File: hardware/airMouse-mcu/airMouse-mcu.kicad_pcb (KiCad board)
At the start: 2 copper layers, 56.5 x 64.5 mm, 115 parts, among them J1 MCU_PRG, J2 RADIO_PRG, J3 AT, J4 DS1020-07-16VBT1A-R, J5 DS1020-07-10VBT1A-R, J6 DS1020-07-4VBT1A-R, Q1 IRLML6346, SW1 KEY, U1 LSM6DS3TR-C, U2 MCP1640CT-I/CHY, U3 STM32G071RBTx, U4 ESP32-C3-WROOM-02U

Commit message: updated for kicad 9
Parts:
- R19: value 2k2 -> 0R
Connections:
- C27 pad 1: /mouse/MOUSE_HOME -> /mouse/MOUSE_BACK
- C28 pad 1: /mouse/MOUSE_PRC -> /mouse/MOUSE_FWD
- C30 pad 1: /mouse/MOUSE_BACK -> /mouse/MOUSE_HOME
- C31 pad 1: /mouse/MOUSE_FWD -> /mouse/MOUSE_PRC
- R50 pad 2: /mouse/MOUSE_FWD -> /mouse/MOUSE_PRC
- R51 pad 2: /mouse/MOUSE_BACK -> /mouse/MOUSE_HOME
- R53 pad 2: /mouse/MOUSE_PRC -> /mouse/MOUSE_FWD
- R54 pad 2: /mouse/MOUSE_HOME -> /mouse/MOUSE_BACK
- U3 pad 1: /mouse/MOUSE_FWD -> /mouse/MOUSE_PRC
- U3 pad 2: /mouse/MOUSE_BACK -> /mouse/MOUSE_HOME
- U3 pad 4: /mouse/MOUSE_PRC -> /mouse/MOUSE_FWD
- U3 pad 5: /mouse/MOUSE_HOME -> /mouse/MOUSE_BACK
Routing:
- net /mouse/MOUSE_HOME: track 48.5 -> 27.4 mm
- net /mouse/MOUSE_BACK: track 27.4 -> 48.5 mm
- net /mouse/MOUSE_PRC: track 48.0 -> 28.9 mm
- net /mouse/MOUSE_FWD: track 28.9 -> 48.0 mm

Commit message: dont know, why voltage drops
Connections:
- net /ESP_RST renamed /ESP_EN
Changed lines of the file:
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@@
 	(net 93 "/COL2")
 	(net 94 "/COL1")
-	(net 95 "/ESP_RST")
+	(net 95 "/ESP_EN")
 	(net 96 "/FB")
 	(net 97 "GND")
@@
 			(size 1.5 0.9)
 			(layers "F.Cu" "F.Mask" "F.Paste")
-			(net 95 "/ESP_RST")
+			(net 95 "/ESP_EN")
 			(pinfunction "EN")
 			(pintype "input")
@@
 			(layers "F.Cu" "F.Mask" "F.Paste")
 			(roundrect_rratio 0.25)
-			(net 95 "/ESP_RST")
+			(net 95 "/ESP_EN")
 			(pinfunction "PB15")
 			(pintype "bidirectional")
@@
 			(layers "F.Cu" "F.Mask" "F.Paste")
 			(roundrect_rratio 0.25)
-			(net 95 "/ESP_RST")
+			(net 95 "/ESP_EN")
 			(pintype "passive")
 		)
@@
 			(layers "F.Cu" "F.Mask" "F.Paste")
 			(roundrect_rratio 0.25)
-			(net 95 "/ESP_RST")
+			(net 95 "/ESP_EN")
 			(pintype "passive")
 		)

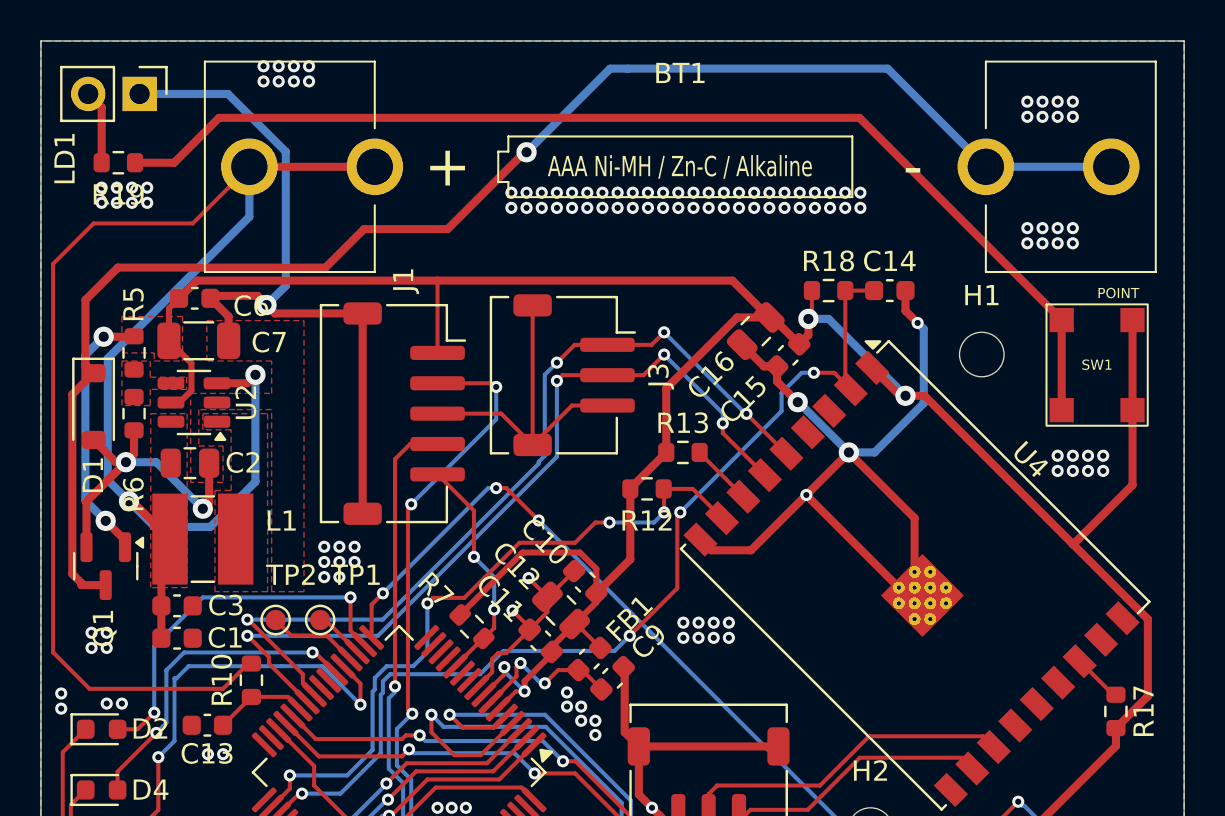
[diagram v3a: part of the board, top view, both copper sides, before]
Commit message: fixed receiving data- overrun turned off
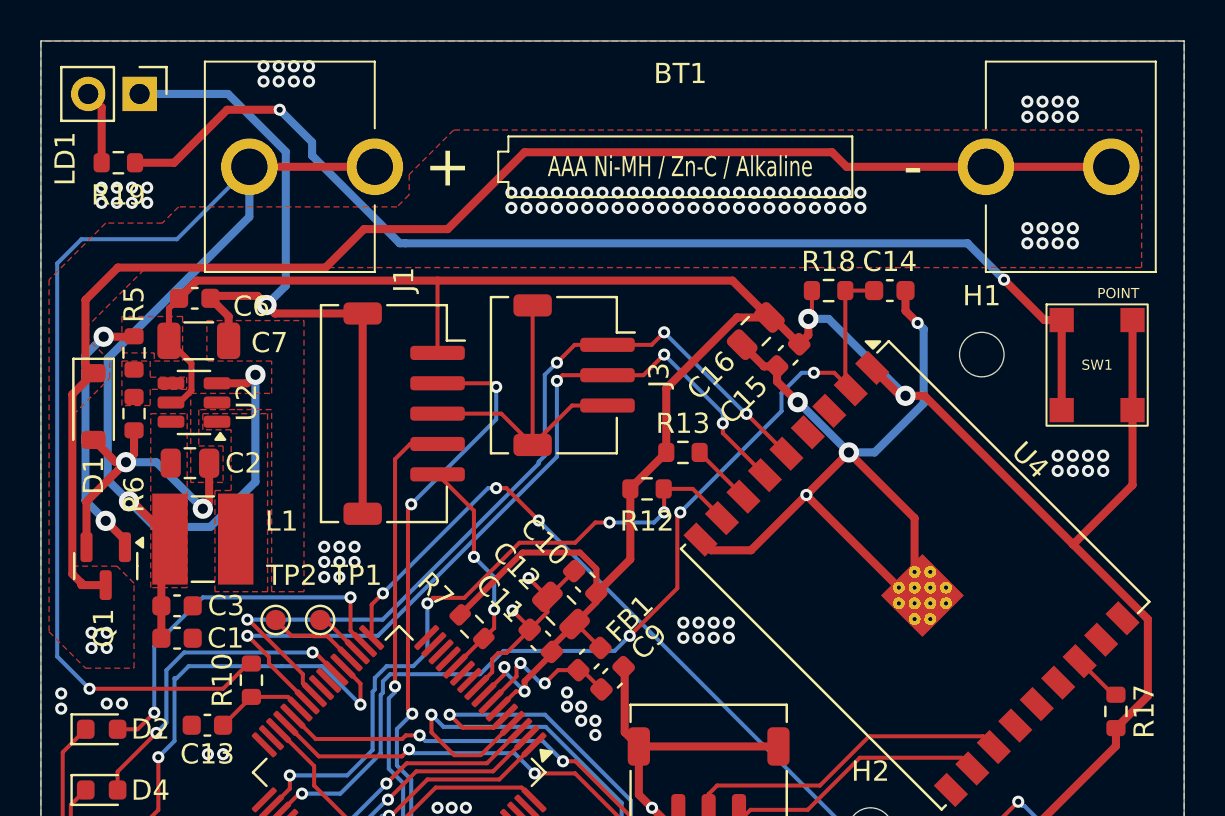
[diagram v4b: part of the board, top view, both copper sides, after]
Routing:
- net /BAT-: track 73.5 -> 70.1 mm, vias 1 -> 0
- net Net-(SW1-A): track 55.5 -> 56.3 mm, vias 0 -> 2
- net /BAT+: track 90.9 -> 90.6 mm, vias 2 -> 3
- added copper zone on F.Cu, net /BAT-

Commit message: new mcu pcb
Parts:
- removed C17, C18, C19, C20, C21, C22, C23, C24, C25, C26, C27, C28, C29, C30, C31, C32, C33, C34, C35, C36: 100n, Capacitor_SMD:C_0603_1608Metric
- removed H1, H2, H3: MountingHole, MountingHole:MountingHole_2.2mm_M2_ISO14580
- removed J3: AT, airMouseLib:JST_ZH_S3B-ZR-SM4A-TF_1x03-1MP_P1.50mm_Horizontal
- removed R26, R27, R28, R29, R30, R31, R32, R33, R34, R35, R36, R37, R38, R39, R40, R41, R42, R43, R44, R45, R46, R47, R48, R49, R50, R51, R52, R53, R54: 10k, Resistor_SMD:R_0603_1608Metric
- removed U4: ESP32-C3-WROOM-02U, RF_Module:ESP32-C3-WROOM-02U
- added C8: 100n, Capacitor_SMD:C_0603_1608Metric, B.Cu at (142.2, 113.6)
- added R55: 0R, Resistor_SMD:R_0603_1608Metric, F.Cu at (142.4, 78.2)
- added TP3: AT_MCU_RX, TestPoint:TestPoint_Pad_D1.0mm, F.Cu at (176.9, 90.5)
- added TP4: AT_MCU_TX, TestPoint:TestPoint_Pad_D1.0mm, F.Cu at (176.9, 93.6)
- added U5: ESP32-C3-WROOM-02, RF_Module:ESP32-C3-WROOM-02, F.Cu at (154.3, 83.8)
- C10, C11, C12, C14, C15, C16, C4, C5, C9, FB1, J2, J5, J6, R1, R11, R12, R13, R17, R19, R2, R25, R3, R4, R7, R8, R9, SW1, TP1, TP2, U1, U3: moved to B.Cu
- C7: footprint Capacitor_SMD:C_1206_3216Metric -> Capacitor_SMD:C_0805_2012Metric
- R18: value 10k -> 10k(NM); moved to B.Cu
- R5: value 976k -> 1M
- R6: value 562k -> 180k
- U2: value MCP1640CT-I/CHY -> TLV61070ADBV
- moved TP2 69.4 mm to (176.8, 84.9)
- moved D2 68.8 mm to (166.4, 87.2)
- moved D3 68.8 mm to (166.4, 93.2)
- moved D4 68.8 mm to (166.4, 90.2)
- moved R14 67.8 mm to (166.3, 100.9), turned to 180 degrees
- moved R16 66.7 mm to (166.3, 102.5), turned to 180 degrees
- moved R15 65.8 mm to (166.3, 104.1), turned to 180 degrees
- moved TP1 65.3 mm to (174.6, 84.9)
- moved LD1 61.6 mm to (166.4, 79.6), turned to 0 degrees
- moved R19 58.7 mm to (162.4, 82.2), turned to 180 degrees
- moved C13 53.0 mm to (157.8, 95.1)
- moved R11 52.6 mm to (162.5, 102.7), turned to -135 degrees
- moved R10 50.7 mm to (157.8, 93.6), turned to 180 degrees
- moved D1 48.4 mm to (150.7, 103.6), turned to 90 degrees
- moved Q1 48.0 mm to (150.1, 95.7), turned to 90 degrees
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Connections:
- C10 pad 1: +3V3 -> /MCU_3V3
- C11 pad 1: +3V3 -> /MCU_3V3
- C12 pad 1: +3V3 -> /MCU_3V3
- C15 pad 1: +3V3 -> /ESP_3V3
- C16 pad 1: +3V3 -> /ESP_3V3
- C4 pad 1: +3V3 -> /SENSOR_3V3
- C5 pad 1: +3V3 -> /SENSOR_3V3
- FB1 pad 1: +3V3 -> /MCU_3V3
- J4 pad 10: /Keyboard/COL6 -> /COL6
- J4 pad 11: /Keyboard/COL5 -> /COL5
- J4 pad 12: /Keyboard/COL4 -> /COL4
- J4 pad 13: /Keyboard/COL3 -> /COL3
- J4 pad 14: /Keyboard/COL2 -> /COL2
- J4 pad 15: /Keyboard/COL1 -> /COL1
- J4 pad 6: /Keyboard/COL10 -> /COL10
- J4 pad 7: /Keyboard/COL9 -> /COL9
- J4 pad 8: /Keyboard/COL8 -> /COL8
- J4 pad 9: /Keyboard/COL7 -> /COL7
- J5 pad 2: /mouse/HOME -> /mouse/MOUSE_DPI
- J5 pad 3: /mouse/PRECISION -> /mouse/MOUSE_HOME
- J5 pad 4: /mouse/DPI -> /mouse/MOUSE_PRC
- J5 pad 5: /mouse/SCRLDN -> /mouse/MOUSE_DN
- J5 pad 6: /mouse/SCRLUP -> /mouse/MOUSE_UP
- J5 pad 7: /mouse/RMB -> /mouse/MOUSE_RB
- J5 pad 8: /mouse/MMB -> /mouse/MOUSE_MB
- J5 pad 9: /mouse/LMB -> Net-(J5-Pin_9)
- J6 pad 2: /mouse/BACK -> /mouse/MOUSE_BACK
- J6 pad 3: /mouse/FWD -> /mouse/MOUSE_FWD
- R1 pad 1: +3V3 -> /SENSOR_3V3
- R12 pad 1: +3V3 -> /ESP_3V3
- R13 pad 1: +3V3 -> /ESP_3V3
- R17 pad 1: +3V3 -> /ESP_3V3
- R18 pad 1: +3V3 -> /ESP_3V3
- R25 pad 1: +3V3 -> Net-(J5-Pin_9)
- R25 pad 2: /Keyboard/COL1 -> /mouse/MOUSE_LB
- R3 pad 1: /SDX -> +3V3
- R3 pad 2: GND -> /MCU_3V3
- R4 pad 1: /SCX -> +3V3
- R4 pad 2: GND -> /SENSOR_3V3
- R7 pad 1: +3V3 -> /MCU_3V3
- R8 pad 1: +3V3 -> /MCU_3V3
- R9 pad 1: +3V3 -> /MCU_3V3
- U1 pad 2: /SDX -> GND
- U1 pad 3: /SCX -> GND
- U1 pad 5: +3V3 -> /SENSOR_3V3
- U1 pad 8: +3V3 -> /SENSOR_3V3
- U3 pad 6: +3V3 -> /MCU_3V3
- U3 pad 8: +3V3 -> /MCU_3V3
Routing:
- net GND: track 280.0 -> 39.7 mm, vias 183 -> 7
- net +3V3: track 247.0 -> 102.6 mm, vias 13 -> 7
- net /SCL: track 96.4 -> 24.4 mm, vias 6 -> 1
- net /BAT-: track 70.1 -> 12.3 mm
- net /SDA: track 88.5 -> 30.9 mm, vias 6 -> 0
- net /BAT+: track 90.6 -> 34.8 mm, vias 3 -> 2
- net /mouse/MOUSE_BACK: track 48.5 -> 0.00 mm, vias 2 -> 0
- net /mouse/MOUSE_FWD: track 48.0 -> 0.00 mm, vias 2 -> 0
- net /MCU_3V3: track 0.00 -> 44.2 mm, vias 0 -> 4
- net Net-(SW1-A): track 56.3 -> 12.2 mm, vias 2 -> 0
- net /mouse/MOUSE_LB: track 27.7 -> 71.2 mm, vias 2 -> 0
- net /ESP_3V3: track 0.00 -> 36.8 mm, vias 0 -> 5
- net /mouse/MOUSE_RB: track 20.5 -> 53.7 mm
- net /SWDCLK: track 34.3 -> 2.40 mm, vias 4 -> 0
- net /mouse/MOUSE_MB: track 25.0 -> 55.7 mm, vias 2 -> 0
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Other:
- board size 56.5 x 64.5 mm -> 36.2 x 52 mm
- board text removed: "C17- C26"
- board text removed: "C29- C36"
- board text removed: "R20-R24"
- board text removed: "R25- R34"
- board text removed: "R35- R44"
- board text removed: "R45- R52"

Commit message: new mcu-pcb
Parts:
- TP3, TP4: moved to B.Cu
- moved TP4 36.6 mm to (141.3, 85.1)
- moved TP3 34.5 mm to (142.6, 86.9)
- moved TP2 12.3 mm to (164.8, 87.5)
- moved TP1 11.2 mm to (163.4, 85.7)
- moved Logo1 9.21 mm to (144.8, 104.6)
- moved R12 8.04 mm to (139.5, 79.0), turned to 180 degrees
- moved D3 4.80 mm to (166.4, 88.4)
- moved D4 3.45 mm to (166.4, 86.8)
- moved R14 3.18 mm to (163.6, 102.5), turned to -90 degrees
- moved D2 2.10 mm to (166.4, 85.1)
- moved R15 1.66 mm to (166.8, 102.5), turned to -90 degrees
- moved R11 1.20 mm to (163.5, 102.0)
- moved R16 1.15 mm to (165.2, 102.5), turned to -90 degrees
- moved BT1 0.80 mm to (138.0, 103.1)
- moved SW1 0.40 mm to (153.8, 80.0)
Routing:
- net /mouse/MOUSE_HOME: track 5.60 -> 85.4 mm, vias 1 -> 4
- net +3V3: track 102.6 -> 145.6 mm, vias 7 -> 9
- net /PRG_ESP_RX: track 0.00 -> 41.6 mm, vias 0 -> 3
- net /mouse/MOUSE_FWD: track 0.00 -> 41.2 mm, vias 0 -> 2
- net /mouse/MOUSE_BACK: track 0.00 -> 40.7 mm, vias 0 -> 2
- net /PRG_ESP_TX: track 0.00 -> 39.0 mm, vias 0 -> 3
- net GND: track 39.7 -> 68.9 mm, vias 7 -> 108
- net /RST: track 1.97 -> 30.2 mm, vias 0 -> 1
- net /Keyboard/KEY_ROW5: track 0.00 -> 25.7 mm, vias 0 -> 1
- net /Keyboard/KEY_ROW4: track 0.00 -> 24.8 mm, vias 0 -> 1
- net /Keyboard/KEY_ROW3: track 0.00 -> 24.3 mm, vias 0 -> 1
- net /Keyboard/KEY_ROW2: track 0.00 -> 23.8 mm, vias 0 -> 1
- net /Keyboard/KEY_ROW1: track 0.00 -> 23.4 mm, vias 0 -> 1
- net /SWDCLK: track 2.40 -> 24.2 mm, vias 0 -> 1
- net /SWDIO: track 0.00 -> 19.7 mm, vias 0 -> 1
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- added copper zone on B.Cu, net /ESP_3V3
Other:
- board size 36.2 x 52 mm -> 36.2 x 53 mm
- board text added: "Neuro Glider v1.0"
- board text removed: "airMouse-mcu"
